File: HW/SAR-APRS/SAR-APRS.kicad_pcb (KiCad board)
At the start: 2 copper layers, 50 x 100 mm, 89 parts, among them J1 uFl, J2 USB_B_Mini, J3 JTAG, J4 uFl, J5 OLED, J6 HEADER_1x02, Q1 2N7002, Q2 2N7002, Q3 2N7002, SW1 SW_DPST_x2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

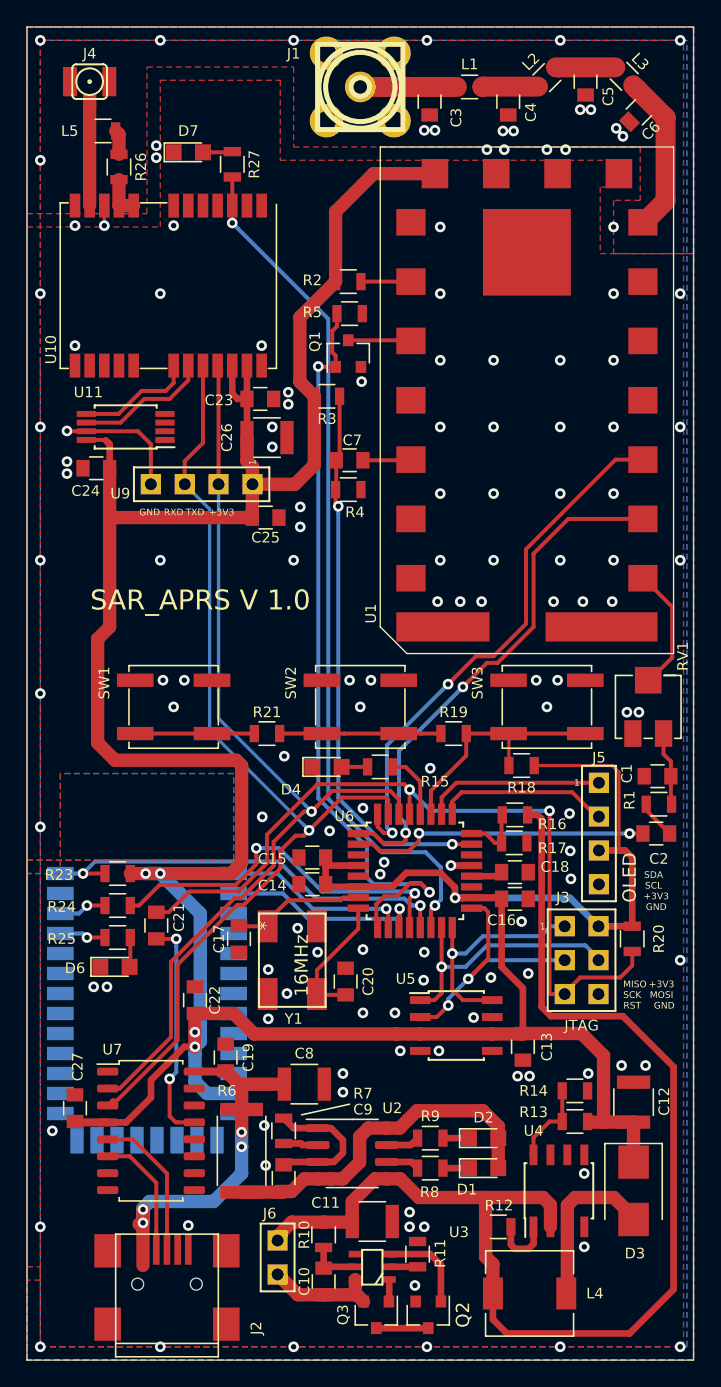
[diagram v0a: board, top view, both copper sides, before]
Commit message: DC-DC changed, PCB update
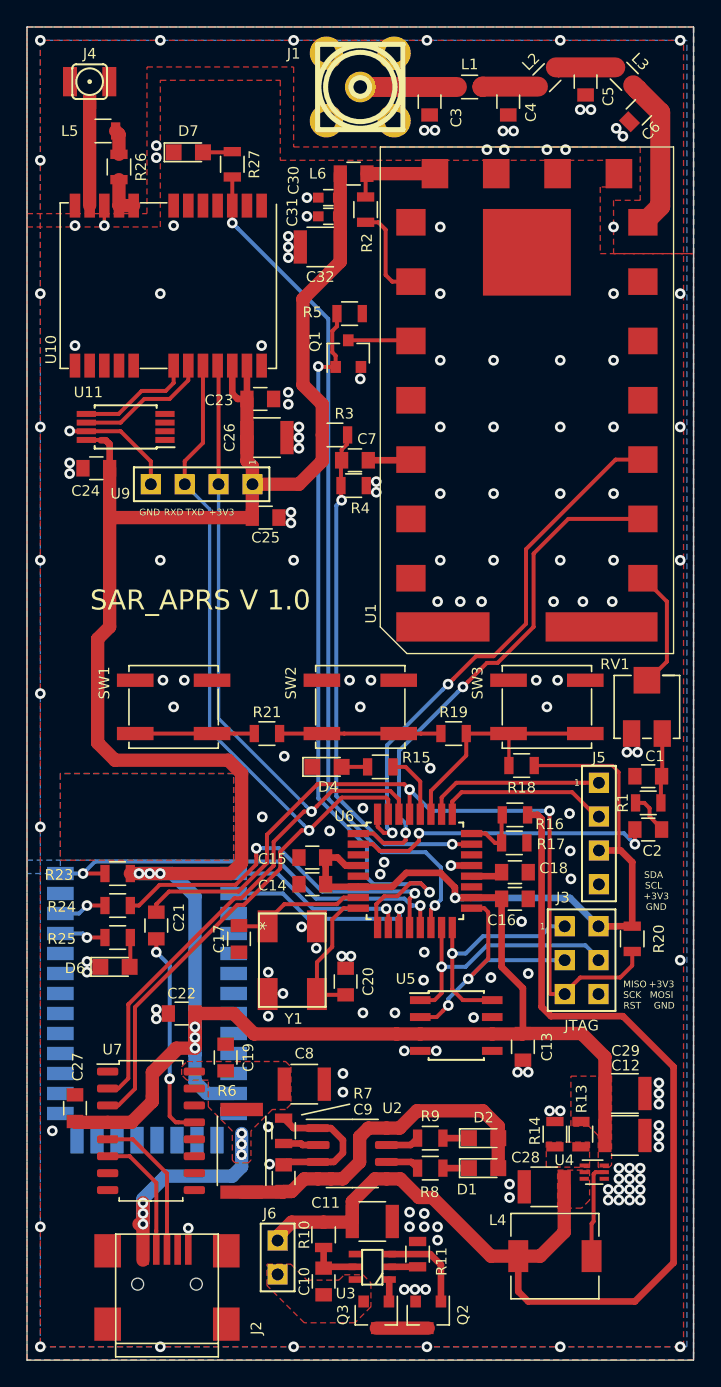
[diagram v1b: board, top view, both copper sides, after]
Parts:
- removed D3: MBRS130T3G, Diodes_SMD:D_SMB
- removed R12: ?, Resistors_SMD:R_0805
- added C28: 10uF, Capacitors_SMD:C_1210, F.Cu at (138.8, 137.0)
- added C29: 22uF, Capacitors_SMD:C_1210, F.Cu at (144.8, 133.2)
- added C30: 100pF, Capacitors_SMD:C_0603, F.Cu at (122.6, 62.8)
- added C31: 10nF, Capacitors_SMD:C_0603, F.Cu at (122.6, 64.2)
- added C32: 10uF, Capacitors_SMD:C_1210, F.Cu at (122.0, 66.5)
- added L6: MPZ2012S601AT, Capacitors_SMD:C_0805, F.Cu at (124.5, 61.0)
- C12: value 10uF -> 22uF
- J5: value OLED -> HEADER_1x04
- L4: value 22uH -> 1uH
- R13: value 2k4 -> ?
- R14: value 1k5 -> ?
- U1: value U1 -> DRA818V
- U4: value ADP1108AN-3.3 -> TPS61023; footprint Housings_SOIC:SOIC-8_3.9x4.9mm_Pitch1.27mm -> Package_TO_SOT_SMD2:SOT-563
- moved R2 5.55 mm to (125.4, 63.7), turned to 90 degrees
- moved R14 3.58 mm to (139.6, 133.1), turned to 270 degrees
- moved L4 3.38 mm to (139.6, 142.2)
- moved U4 3.00 mm to (142.6, 135.9), turned to 0 degrees
- moved R3 2.96 mm to (123.1, 80.6)
- moved C22 1.41 mm to (111.6, 124.0), turned to 0 degrees
- moved R13 1.05 mm to (141.6, 133.1), turned to 90 degrees
- moved C12 0.92 mm to (144.8, 130.0), turned to 0 degrees
- moved R1 0.81 mm to (146.6, 108.2)
- moved C1 0.70 mm to (146.6, 106.2)
- moved C2 0.67 mm to (146.6, 110.2)
- moved R4 0.50 mm to (124.5, 84.4)
- moved C7 0.40 mm to (124.6, 82.5)
- moved RV1 0.10 mm to (146.5, 101.0)
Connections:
- L4 pad 2: Net-(D3-Pad2) -> Net-(L4-Pad2)
- R2 pad 2: +3V3 -> Net-(L6-Pad2)
- U1 pad 8: +3V3 -> Net-(L6-Pad2)
- U4 pad 1: Net-(R12-Pad1) -> Net-(R13-Pad1)
- U4 pad 3: Net-(D3-Pad2) -> Bat+
- U4 pad 5: GND -> Net-(L4-Pad2)
- U4 pad 6: Net-(U4-Pad6) -> +3V3
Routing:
- net Net-(D3-Pad2): track 12.6 -> 0.00 mm
- net /CPU/VUSB: track 28.0 -> 17.1 mm, vias 4 -> 6
- net Bat-: track 8.53 -> 0.00 mm
- net Net-(L4-Pad2): track 0.00 -> 7.07 mm
- net Net-(L6-Pad2): track 0.00 -> 6.89 mm
- net Net-(R13-Pad1): track 6.31 -> 0.00 mm
- net Bat+: track 94.4 -> 88.6 mm
- net Net-(R12-Pad1): track 4.60 -> 0.00 mm
- net Net-(R2-Pad1): track 3.75 -> 7.23 mm
- net +3V3: track 257.6 -> 254.8 mm, vias 5 -> 7
- net /CPU/RFMOD_AUX: track 41.8 -> 39.4 mm
- net Net-(C21-Pad2): track 17.0 -> 15.8 mm
- net GND: track 24.5 -> 23.5 mm, vias 138 -> 173
- net /CPU/RFMOD_MIC: track 22.4 -> 23.3 mm
- net Net-(C20-Pad2): track 9.97 -> 10.6 mm
- added copper zone on F.Cu, net +3V3
- added copper zone on F.Cu, net /CPU/VUSB
- added copper zone on F.Cu, net Bat+
- added copper zone on F.Cu, net Bat-
- added copper zone on F.Cu, net Net-(R13-Pad1)
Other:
- rule pad_to_mask_clearance: 0.2 -> 0

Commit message: ibom added
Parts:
- R13: value ? -> 500k
- R14: value ? -> 110k
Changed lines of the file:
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@@
       (effects (font (size 0.8 0.8) (thickness 0.15)))
     )
-    (fp_text value ? (at 0 1.75 90) (layer F.Fab) hide
+    (fp_text value 500k (at 0 1.75 90) (layer F.Fab) hide
       (effects (font (size 1 1) (thickness 0.15)))
     )
@@
       (effects (font (size 0.8 0.8) (thickness 0.15)))
     )
-    (fp_text value ? (at 0 1.75 270) (layer F.Fab) hide
+    (fp_text value 110k (at 0 1.75 270) (layer F.Fab) hide
       (effects (font (size 1 1) (thickness 0.15)))
     )
